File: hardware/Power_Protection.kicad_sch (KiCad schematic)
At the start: 17 parts, among them U7 LM76202QPWPRQ1

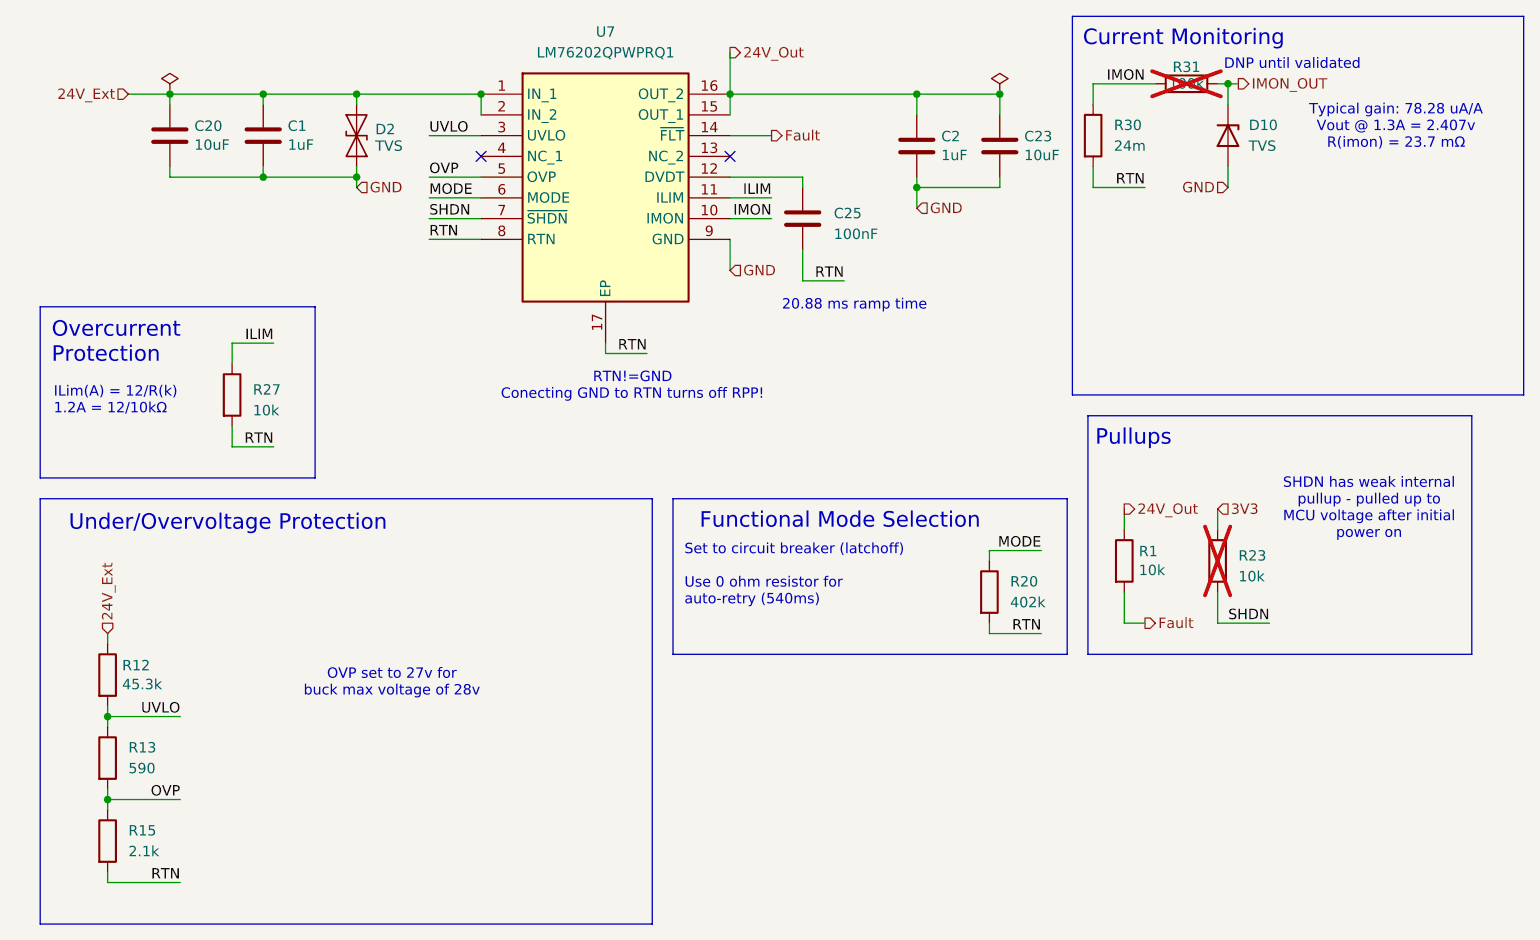
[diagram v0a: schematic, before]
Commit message: some changes - switched to contactor design block - switched to power protection design block - added SD card - added fan I2C pullup - added resistors for ESP32 power mux - shield tied to gnd with 0 ohm - added USB-PD and boost design blocks
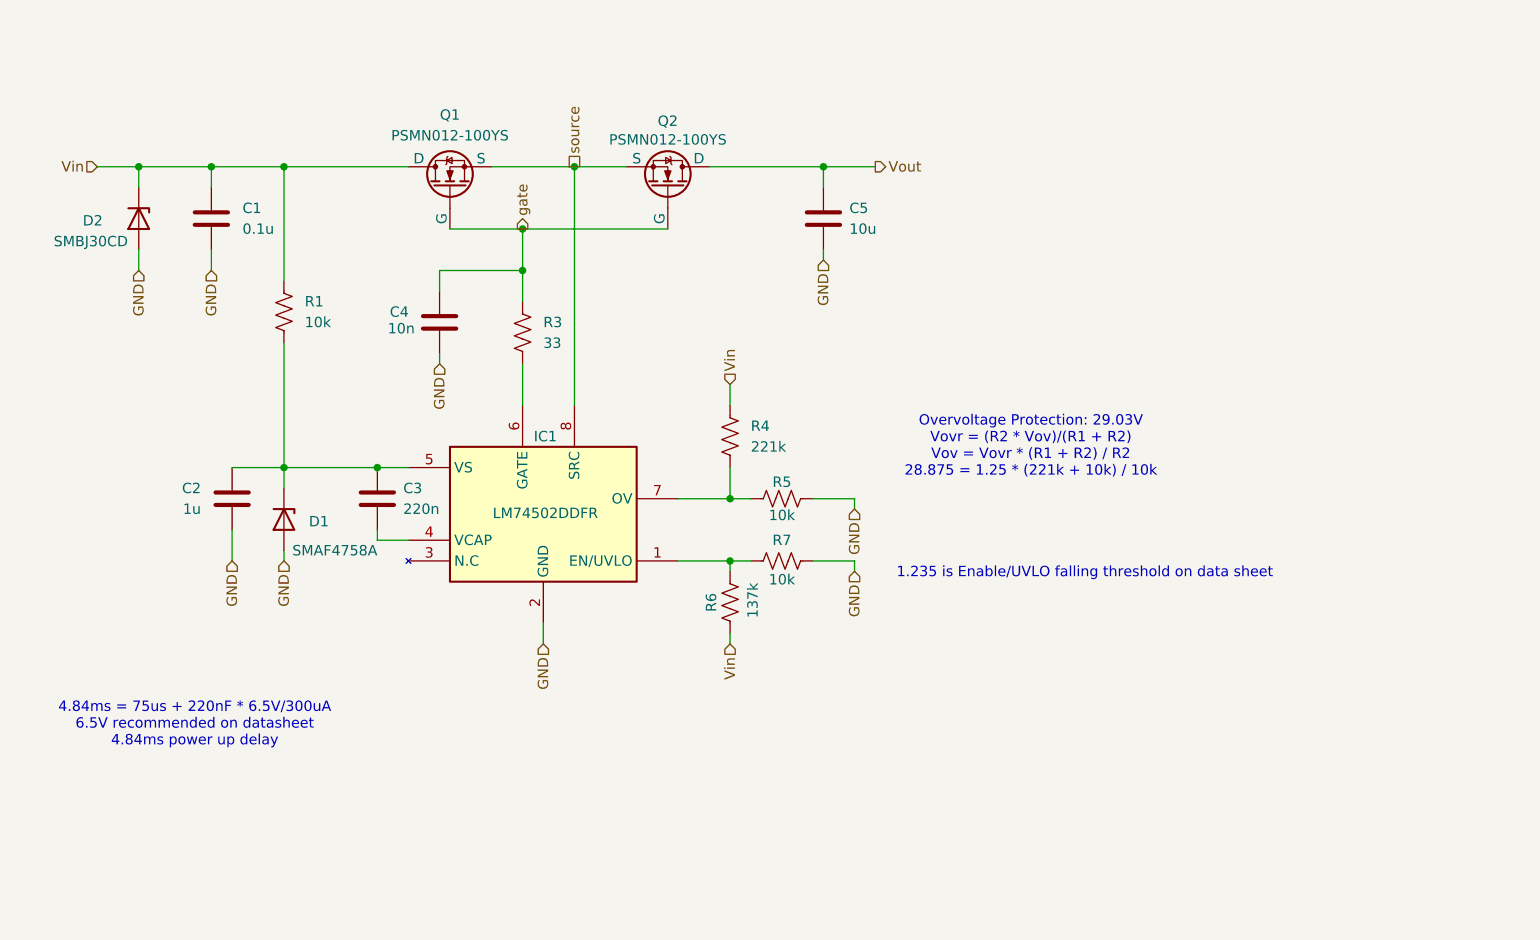
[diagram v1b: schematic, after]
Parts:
- removed C20, C23: 10uF, Capacitor_SMD:C_0805_2012Metric_Pad1.18x1.45mm_HandSolder, symbol Device:C
- removed C25: 100nF, Capacitor_SMD:C_0603_1608Metric_Pad1.08x0.95mm_HandSolder, symbol Device:C
- removed D10: TVS, Diode_SMD:D_SOD-123F, symbol Device:D_Zener
- removed D2: TVS, Diode_SMD:D_SOD-323_HandSoldering, symbol Diode:SD12_SOD323
- removed R1, R23, R27: 10k, Resistor_SMD:R_0603_1608Metric_Pad0.98x0.95mm_HandSolder, symbol Device:R
- removed R12: 45.3k, Resistor_SMD:R_0603_1608Metric_Pad0.98x0.95mm_HandSolder, symbol Device:R
- removed R13: 590, Resistor_SMD:R_0603_1608Metric_Pad0.98x0.95mm_HandSolder, symbol Device:R
- removed R15: 2.1k, Resistor_SMD:R_0603_1608Metric_Pad0.98x0.95mm_HandSolder, symbol Device:R
- removed R20: 402k, Resistor_SMD:R_0603_1608Metric_Pad0.98x0.95mm_HandSolder, symbol Device:R
- removed R30: 24m, Resistor_SMD:R_0603_1608Metric_Pad0.98x0.95mm_HandSolder, symbol Device:R
- removed R31: 100k, Resistor_SMD:R_0603_1608Metric_Pad0.98x0.95mm_HandSolder, symbol Device:R
- removed U7: LM76202QPWPRQ1, LHRS_Power:LM76202QPWPRQ1, symbol lhrs_power:LM76202QPWPRQ1
- added C3: 220n, Capacitor_SMD:C_0603_1608Metric_Pad1.08x0.95mm_HandSolder, symbol Device:C
- added C4: 10n, Capacitor_SMD:C_0603_1608Metric_Pad1.08x0.95mm_HandSolder, symbol ECE319H:C
- added C5: 10u, Capacitor_SMD:C_0603_1608Metric_Pad1.08x0.95mm_HandSolder, symbol Device:C
- added D1: SMAF4758A, UTSVT_Passives:SODFL5026X125N, symbol Device:D_Zener
- added D2: SMBJ30CD, UTSVT_Power:SMBJ30CD, symbol Device:D_Zener
- added IC1: LM74502DDFR, UTSVT_Power:LM74502DDFR, symbol UTSVT_ICs:LM74502HDDFR
- added Q1, Q2: PSMN012-100YS, UTSVT_Power:PSMN012-100YS, symbol utsvt_power:PSMN012-100YS
- added R1, R5, R7: 10k, Resistor_SMD:R_0603_1608Metric_Pad0.98x0.95mm_HandSolder, symbol Device:R_US
- added R3: 33, Resistor_SMD:R_0603_1608Metric_Pad0.98x0.95mm_HandSolder, symbol Device:R_US
- added R4: 221k, Resistor_SMD:R_0603_1608Metric_Pad0.98x0.95mm_HandSolder, symbol Device:R_US
- added R6: 137k, Resistor_SMD:R_0603_1608Metric_Pad0.98x0.95mm_HandSolder, symbol Device:R_US
- C1: value 1uF -> 0.1u; LCSC P/N (none) -> C14663; P/N MLASU168SB5105KTNA01 -> MLASH168SB7104KTNA01
- C2: value 1uF -> 1u; LCSC P/N (none) -> C15849
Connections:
- net 24V_Out is gone; now on net GND: C2.1
- net GND: now also C4.2, C5.2, D1.2 (A), D2.2 (A), IC1.2 (GND), R5.2, R7.2; no longer C2.2
- net 24V_Ext renamed Vin
- net Vin: now also D2.1 (K), Q1.1 (D), R1.2, R4.1, R6.2
- new net: C2.2, C3.1, D1.1 (K), IC1.5 (VS), R1.1
- new net: C3.2, IC1.4 (VCAP)
- new net: IC1.1 (EN/UVLO), R6.1, R7.1
- new net: IC1.6 (GATE), R3.2
- new net: IC1.7 (OV), R4.2, R5.1
- new net Vout: C5.1, Q2.1 (D)
- new net gate: C4.1, Q1.2 (G), Q2.2 (G), R3.1
- new net source: IC1.8 (SRC), Q1.3 (S), Q2.3 (S)
- no-connect marks 2 -> 0
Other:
- note added: "1.235 is Enable/UVLO falling threshold on data sheet"
- note added: "4.84ms = 75us + 220nF * 6.5V/300uA 6.5V recommended on datasheet 4.84ms power up delay"
- note added: "Overvoltage Protection: 29.03V Vovr = (R2 * Vov)/(R1 + R2) Vov = Vovr * (R1 + R2) / R2 28.875 = 1.25 * (221k + 10k) / 10k"
- note removed: "20.88 ms ramp time"
- note removed: "Current Monitoring"
- note removed: "DNP until validated"
- note removed: "Functional Mode Selection"
- note removed: "ILim(A) = 12/R(k) 1.2A = 12/10kΩ"
- note removed: "OVP set to 27v for buck max voltage of 28v"
- note removed: "Overcurrent Protection"
- note removed: "Pullups"
- note removed: "RTN!=GND Conecting GND to RTN turns off RPP!"
- note removed: "SHDN has weak internal pullup - pulled up to MCU voltage after initial power on"
- note removed: "Set to circuit breaker (latchoff) Use 0 ohm resistor for auto-retry (540ms)"
- note removed: "Typical gain: 78.28 uA/A Vout @ 1.3A = 2.407v R(imon) = 23.7 mΩ"
- note removed: "Under/Overvoltage Protection"

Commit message: 🗿
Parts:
- R1, R3, R4, R5, R6, R7: symbol Device:R_US -> Device:R
